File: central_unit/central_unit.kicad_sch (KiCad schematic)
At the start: 34 parts, among them J1 5V_in, J2 OLED Display, J3 LIPO_in, J4 MicroSD holder, J5 HDMI_A, J6 no_fit, U1 Pico_SMD_NODEBUG, U2 TXS0108EPW, U3 SIM800L-CORE, U4 MIC29302WU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

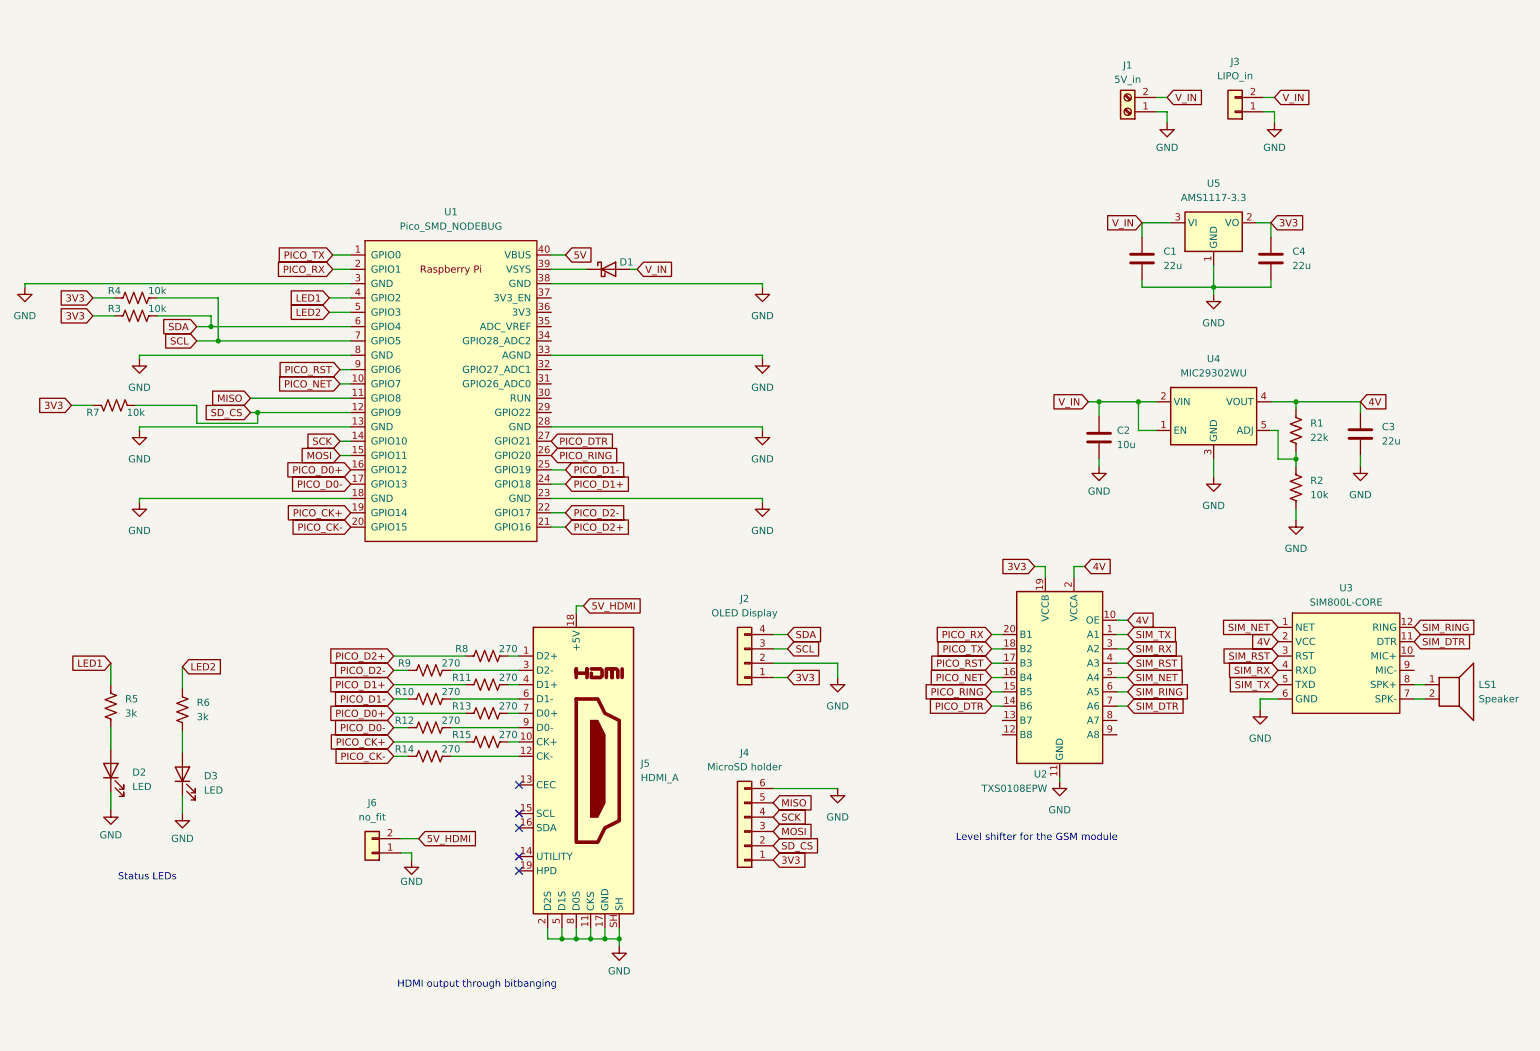
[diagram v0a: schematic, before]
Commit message: Complete routing of sensing unit
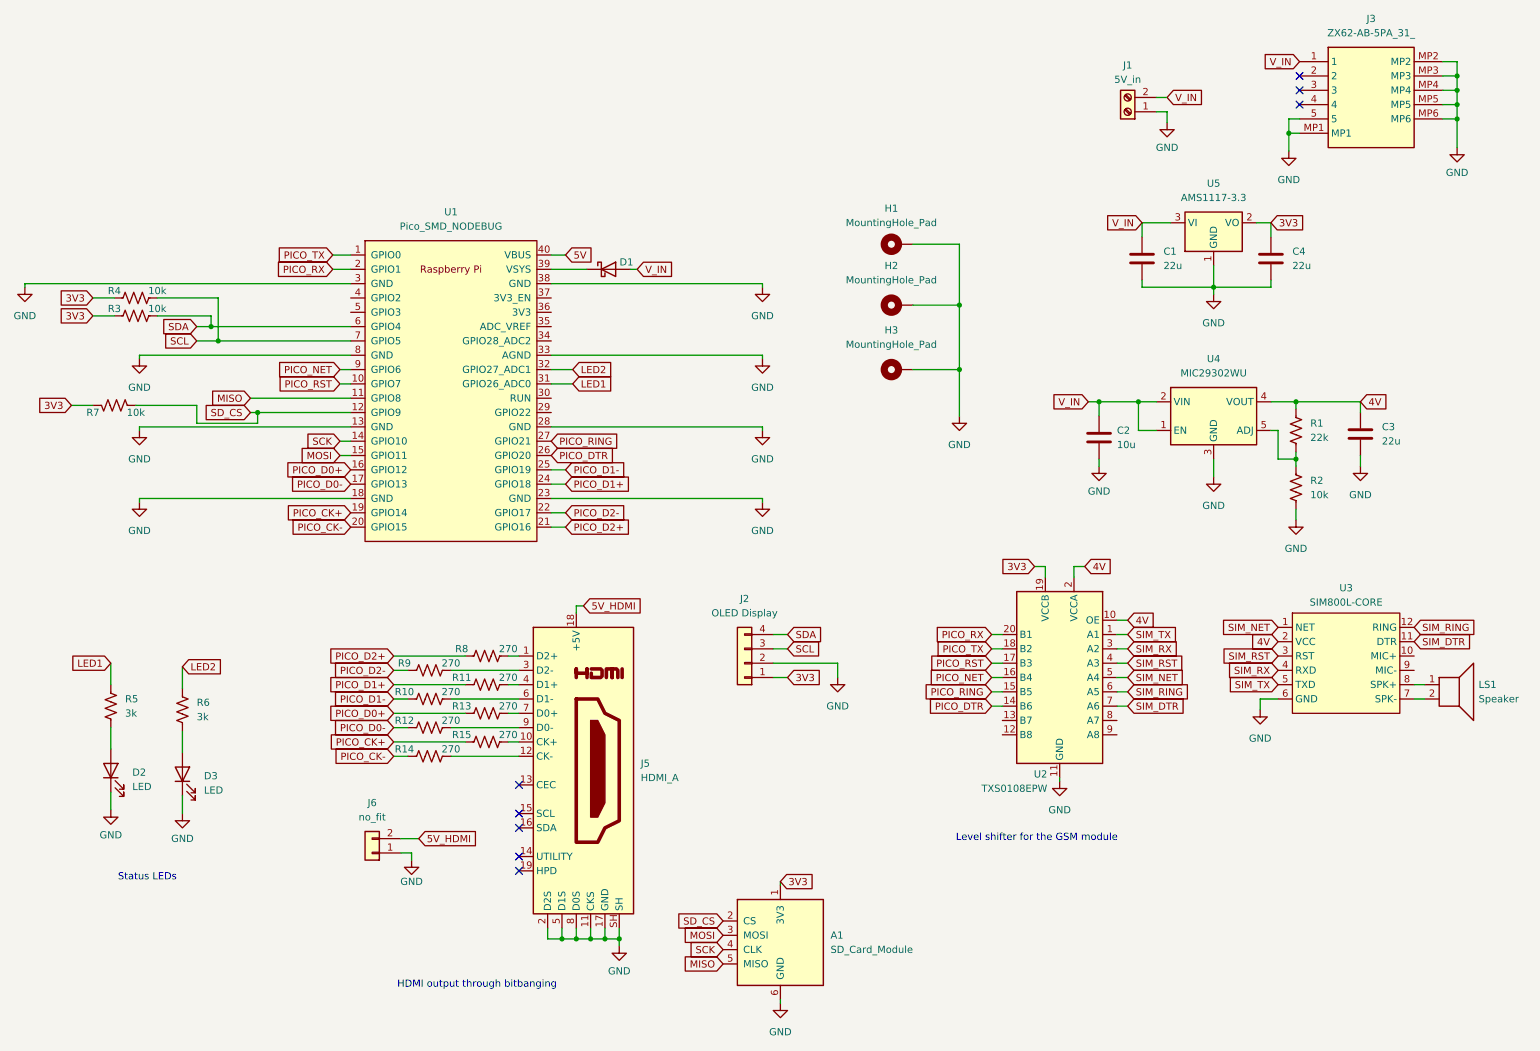
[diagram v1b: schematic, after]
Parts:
- removed J3: LIPO_in, symbol Connector_Generic:Conn_01x02
- removed J4: MicroSD holder, symbol Connector_Generic:Conn_01x06
- added A1: SD_Card_Module, Charleslabs_Parts:SD_Card_Module, symbol Charleslabs_Parts:SD_Card_Module
- added H1, H2, H3: MountingHole_Pad, MountingHole:MountingHole_3.2mm_M3_Pad_Via, symbol Mechanical:MountingHole_Pad
- added J3: ZX62-AB-5PA_31_, microUSB:ZX62AB5PA31, symbol ZX62-AB-5PA_31_:ZX62-AB-5PA_31_
- C1, C2, C3, C4: footprint (none) -> Capacitor_SMD:C_0805_2012Metric_Pad1.18x1.45mm_HandSolder
- D1: footprint (none) -> Diode_SMD:D_SOD-323_HandSoldering
- D2, D3: footprint (none) -> LED_SMD:LED_0603_1608Metric_Pad1.05x0.95mm_HandSolder
- J1: footprint (none) -> TerminalBlock_Phoenix:TerminalBlock_Phoenix_MKDS-1,5-2_1x02_P5.00mm_Horizontal
- J2: footprint (none) -> SSD1306:128x64OLED
- J5: footprint (none) -> Connector_HDMI:HDMI_A_Molex_208658-1001_Horizontal
- J6: footprint (none) -> Connector_PinHeader_2.54mm:PinHeader_1x02_P2.54mm_Vertical
- LS1: footprint (none) -> Buzzer_Beeper:Buzzer_12x9.5RM7.6
- R1, R10, R11, R12, R13, R14, R15, R2, R3, R4, R5, R6, R7, R8, R9: footprint (none) -> Resistor_SMD:R_0805_2012Metric_Pad1.20x1.40mm_HandSolder
- U3: footprint (none) -> SIM800L:SIM800L-CORE
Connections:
- net 3V3: now also A1.1 (3V3)
- net GND: now also A1.6 (GND), H1.1, H2.1, H3.1, J3.5, J3.MP1, J3.MP2, J3.MP3, J3.MP4, J3.MP5, J3.MP6
- net LED1: now also U1.31 (GPIO26_ADC0); no longer U1.4 (GPIO2)
- net LED2: now also U1.32 (GPIO27_ADC1); no longer U1.5 (GPIO3)
- net MISO: now also A1.5 (MISO)
- net MOSI: now also A1.3 (MOSI)
- net PICO_DTR: now also U1.26 (GPIO20); no longer U1.27 (GPIO21)
- net PICO_NET: now also U1.9 (GPIO6); no longer U1.10 (GPIO7)
- net PICO_RING: now also U1.27 (GPIO21); no longer U1.26 (GPIO20)
- net PICO_RST: now also U1.10 (GPIO7); no longer U1.9 (GPIO6)
- net SCK: now also A1.4 (CLK)
- net SD_CS: now also A1.2 (CS)
- net V_IN: now also J3.1
- no-connect marks 5 -> 8
